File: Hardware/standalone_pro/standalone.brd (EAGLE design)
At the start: 110 x 100 mm, 107 parts, among them IC1 STM32F050C6T6A, IC2 AP1212, IC3 AP1212, Q2 32.768khz, U1 NMOS_2N7002, U10 ZXCT1107SA-7, U2 DMS3016SSS-13, U3 DMS3016SSS-13, U4 LM2576S, U5 NMOS_2N7002, U6 NMOS_2N7002, U7 INA213AIDCKT, U9 PMOS_RSS090P03, X1 KUSBVX, X2 KUSBVX, X3 KUSBVX, X4 KUSBVX

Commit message: Pro Standalone board updated
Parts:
- removed 5V_CIN: 100u, resistor:PANASONIC_E
- removed 5V_COUT: 1000uF, resistor:PANASONIC_G
- removed GATE_DRIVE: IR2104S, equinox:IR2104S
- removed KEY_1, KEY_2, KEY_3: 10K, rcl:M0805
- removed Q2: 32.768khz, equinox:CRYSTAL_CMJ206T
- removed U$2, U$3, U$4, U$5, U$6: KYCON_KLDVX-0202, equinox:KYCON_KLVDX_2020_B
- removed U1: NMOS_2N7002, equinox:SOT103P240X110-3N
- added C21: 100uF, resistor:PANASONIC_E
- added C22: 1000uF, resistor:PANASONIC_G
- added D1: SSB43L, equinox:DO214AA
- added D5: BZX384-C3V6, equinox:SOD323
- added DC1, DC2, DC3, DC4, DC5: KYCON_KLDVX-0202, equinox:KYCON_KLVDX_2020_B
- added IC4: AP1212, equinox:SO8
- added PTC1: 7A, equinox:PTC_MF_R700
- added Q1: 32.768khz, equinox:CRYSTAL_CMJ206T
- added R38: 49.9k, resistor:M0805
- added U11, U12, U8: NMOS_2N7002, equinox:SOT103P240X110-3N
- BUZZ1: device buzzer:14MM_5M_PINS -> equinox:BUZZ_14MM_5M_PINS
- C5: value 0.1uF -> 100nF
- D3: value (none) -> SSB43L
- D4: value US1D - 1625280 -> US1D
- IC3: value AP1212 -> IR2104S; device equinox:SO8 -> equinox:IR2104S
- R1: value 1k -> 75k
- R21: value 1K -> 1k
- R29: value 75k -> 1k
- R31: value 49.9k -> 10M
- R32, R34, R36: value 75k -> 49.9k
- R33, R35, R37: value 49.9k -> 75k
- R4, R6: value 1.32k -> 1.33k
- U2, U3: value DMS3016SSS-13 -> FDS6690a
- moved U4 123.5 mm to (-4.25, 12.2), flipped to the bottom
- moved L_5V 118.2 mm to (-3.00, 38.0), flipped to the bottom
- moved DIS1 106.2 mm to (-3.10, 56.0), flipped to the top
- moved C11 105.0 mm to (-8.00, 69.0), flipped to the bottom
- moved R1 99.8 mm to (-6.00, -18.0), turned to 0 degrees
- moved IC3 97.1 mm to (9.00, 65.0), flipped to the bottom
- moved C2 95.0 mm to (-3.00, 66.0), flipped to the bottom
- moved D2 95.0 mm to (-3.00, 69.0), flipped to the bottom
- moved D4 95.0 mm to (-3.00, 62.0), flipped to the bottom
- moved R29 90.0 mm to (15.0, 51.0), flipped to the bottom
- moved JTAG 86.0 mm to (92.0, 18.0), flipped to the bottom
- moved X3 86.0 mm to (7.00, 25.6), flipped to the top
- moved U2 83.0 mm to (3.00, 75.0), flipped to the bottom
- moved KEYPAD 82.0 mm to (91.0, 36.0), flipped to the bottom
- moved LED1 82.0 mm to (92.0, 7.00), flipped to the bottom
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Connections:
- removed net LCD_PWR: IC1.32, R1.2
- new net N$47: R35.1, R36.2, X4.2
- new net N$48: R37.1, R38.2, X4.3
- net +3V3: no longer KEY_1.2, KEY_2.2, KEY_3.2
- net +5V: now also C22.+, IC4.7; no longer 5V_COUT.+, IC3.7
- net 12V_OUT: now also DC1.1, DC2.1, DC3.1; no longer U$2.1, U$3.1, U$4.1
- net 12V_OUT1: now also DC4.1, DC5.1; no longer U$5.1, U$6.1
- net GND: now also C21.-, C22.-, CONTR.1, D1.A, D5.A, DC1.2, DC1.3, DC2.2, DC2.3, DC3.2, DC3.3, DC4.2, DC4.3, DC5.2, DC5.3, DIS1.1, DIS1.10, DIS1.7, DIS1.8, DIS1.9, IC3.4, IC4.6, Q1.CASE, R32.1, R34.1, R36.1, R38.1, U11.2, U8.2; no longer 5V_CIN.-, 5V_COUT.-, BUZZ1.P$2, GATE_DRIVE.4, IC3.6, Q2.CASE, R31.1, R33.1, R35.1, R37.1, U$4.2, U$5.2, U$5.3, U$6.2, U$6.3, U1.2
- net N$1: now also Q1.P$2; no longer Q2.P$2
- net N$10: now also IC3.8; no longer GATE_DRIVE.8
- net N$13: now also IC3.5; no longer GATE_DRIVE.5
- net N$16: now also IC3.1; no longer GATE_DRIVE.1
- net N$17: now also R33.1, R34.2, X3.3; no longer R1.1, U1.1
- net N$18: now also Q1.P$3; no longer Q2.P$3
- net N$22: now also R29.1; no longer BUZZ1.P$1
- net N$23: no longer KEY_1.1
- net N$24: no longer KEY_2.1
- net N$26: no longer KEY_3.1
- net N$3: now also IC3.3; no longer GATE_DRIVE.3
- net N$4: now also D1.C, PTC1.P$1; no longer BATT.P$1
- net N$42: now also BUZZ1.P$2, U8.3; no longer R29.1, R31.2, X3.2
- net N$43: now also R29.2, U8.1; no longer R32.1, R33.2, X3.3
- net N$44: now also C16.2, R31.2, U11.1; no longer R34.1, R35.2, X4.2
- net N$45: now also U11.3, U12.2; no longer R36.1, R37.2, X4.3
- net N$46: now also BATT.P$1, PTC1.P$2; no longer U$2.2, U$2.3, U$3.2, U$3.3, U$4.3
- net N$5: now also R1.1, R32.2, X3.2; no longer CONTR.1, DIS1.1, DIS1.10, DIS1.7, DIS1.8, DIS1.9, U1.3
- net N$6: now also IC3.6; no longer GATE_DRIVE.6
- net N$7: now also IC3.7; no longer GATE_DRIVE.7
- net N$8: now also IC3.2; no longer GATE_DRIVE.2
- net NRST: now also U12.3
- net SOL_I: now also D5.C
- net USB_EN1: now also IC4.1; no longer IC3.1
- net USB_EN2: now also IC4.4; no longer IC3.4
- net USB_FLG1: now also IC4.2; no longer IC3.2
- net USB_FLG2: now also IC4.3; no longer IC3.3
- net USB_OUT1: now also IC4.8, R1.2, R33.2; no longer IC3.8, R29.2, R32.2
- net USB_OUT2: now also IC4.5, R35.2, R37.2; no longer IC3.5, R34.2, R36.2
- net V_BACKUP: no longer C16.2
- net V_LOAD: now also BUZZ1.P$1, C21.+; no longer 5V_CIN.+
- net WKUP: now also R31.1, U12.1
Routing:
- net V_LOAD: track 316.3 -> 8.97 mm, vias 16 -> 0
- net +5V: track 219.2 -> 0.00 mm, vias 4 -> 0
- net N$21: track 112.7 -> 0.00 mm
- net LCD_PWR: track 51.6 -> 0.00 mm, vias 2 -> 0
- net N$5: track 38.6 -> 0.00 mm, vias 1 -> 0
- net V_BACKUP: track 26.3 -> 55.8 mm, vias 0 -> 1
- net N$12: track 36.5 -> 62.3 mm
- net N$4: track 7.80 -> 30.9 mm
- net NRST: track 53.1 -> 73.8 mm, vias 0 -> 2
- net BATT_V: track 36.8 -> 54.0 mm
- net N$26: track 38.7 -> 25.9 mm
- net N$16: track 148.2 -> 160.5 mm
- net SOL_I: track 74.7 -> 86.7 mm
- net GND: track 76.7 -> 65.2 mm, vias 49 -> 28
- net N$6: track 66.1 -> 54.6 mm
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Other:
- board size 110 x 100 mm -> 110.1 x 100 mm
- board text added: "Designed by Ashley Grealish in London Manufactured in China"
- board text added: "GND"
- board text added: "RX"
- board text added: "TX"
- board text removed: "Design by Ashley Grealish - 2013"

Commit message: Added Relay to Standalone Pro
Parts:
- removed R14: 100K, rcl:M0805
- removed U9: PMOS_RSS090P03, equinox:SO8
- added D7: US1D, diode:DO-214AC
- added U$2: RELAY_G5RL-1E, equinox:G5RL-1E
- added U$3: CON_MOLEX_39_29_1028, equinox:MOLEX_39_29_1028
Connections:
- removed net N$25: R14.1, U5.3, U9.4
- new net N$50: D7.A, U$2.COIL+, U5.3
- net 12V_OUT: now also U$2.NO@1, U$2.NO@2, U$3.P$1; no longer U9.5, U9.6, U9.7, U9.8
- net GND: now also U$3.P$2
- net V_LOAD: now also D7.C, U$2.COM@1, U$2.COM@2; no longer R14.2, U9.1, U9.2, U9.3
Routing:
- net N$25: track 13.3 -> 0.00 mm
- net 12V_OUT: track 71.2 -> 58.7 mm
- net V_LOAD: track 8.97 -> 5.40 mm

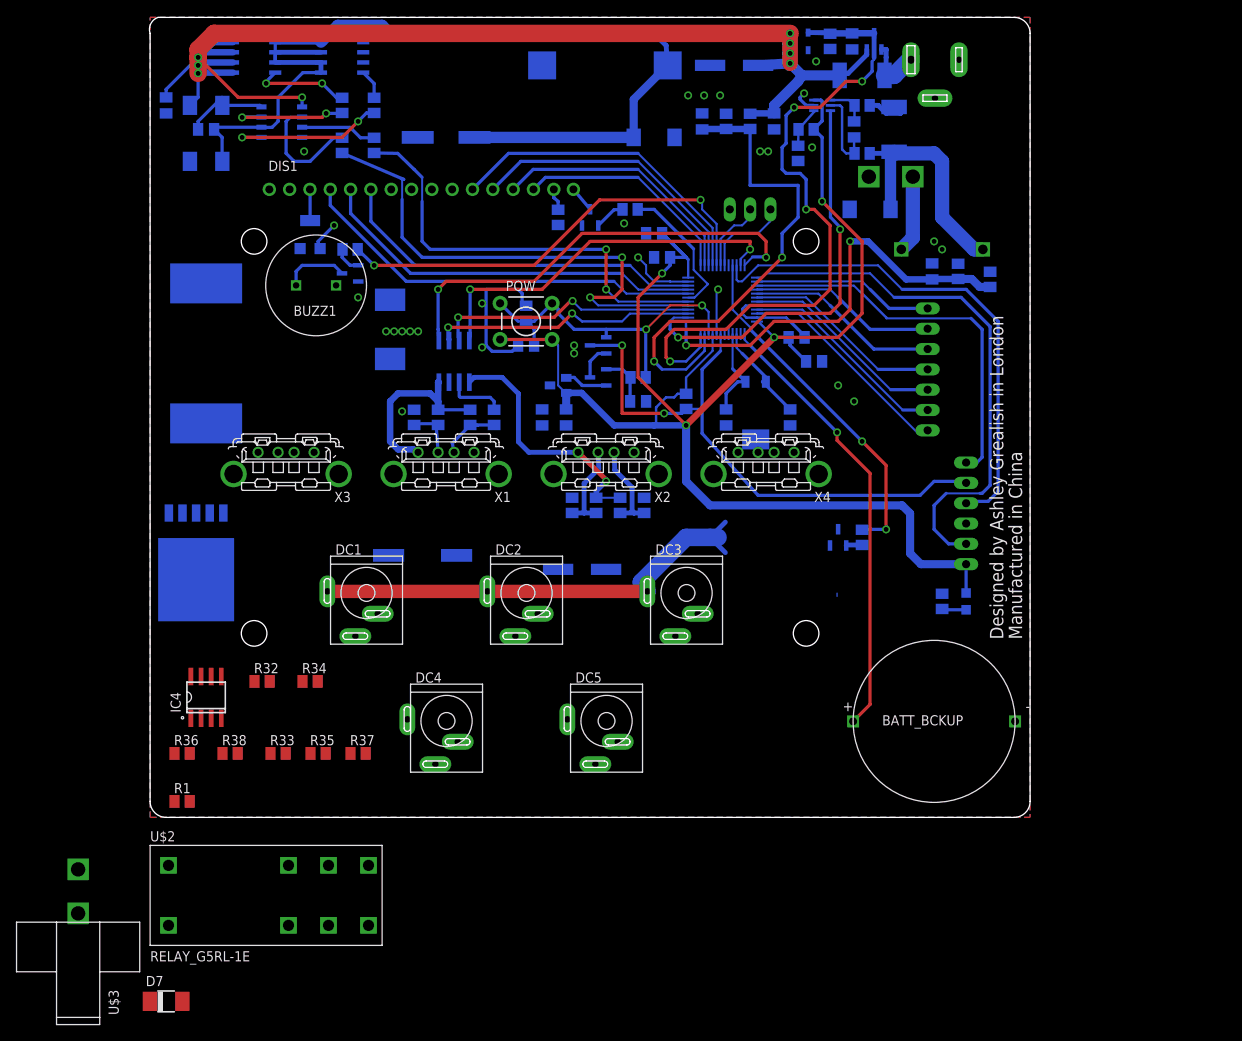
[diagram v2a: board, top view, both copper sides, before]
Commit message: Connections added (with corrected faults)
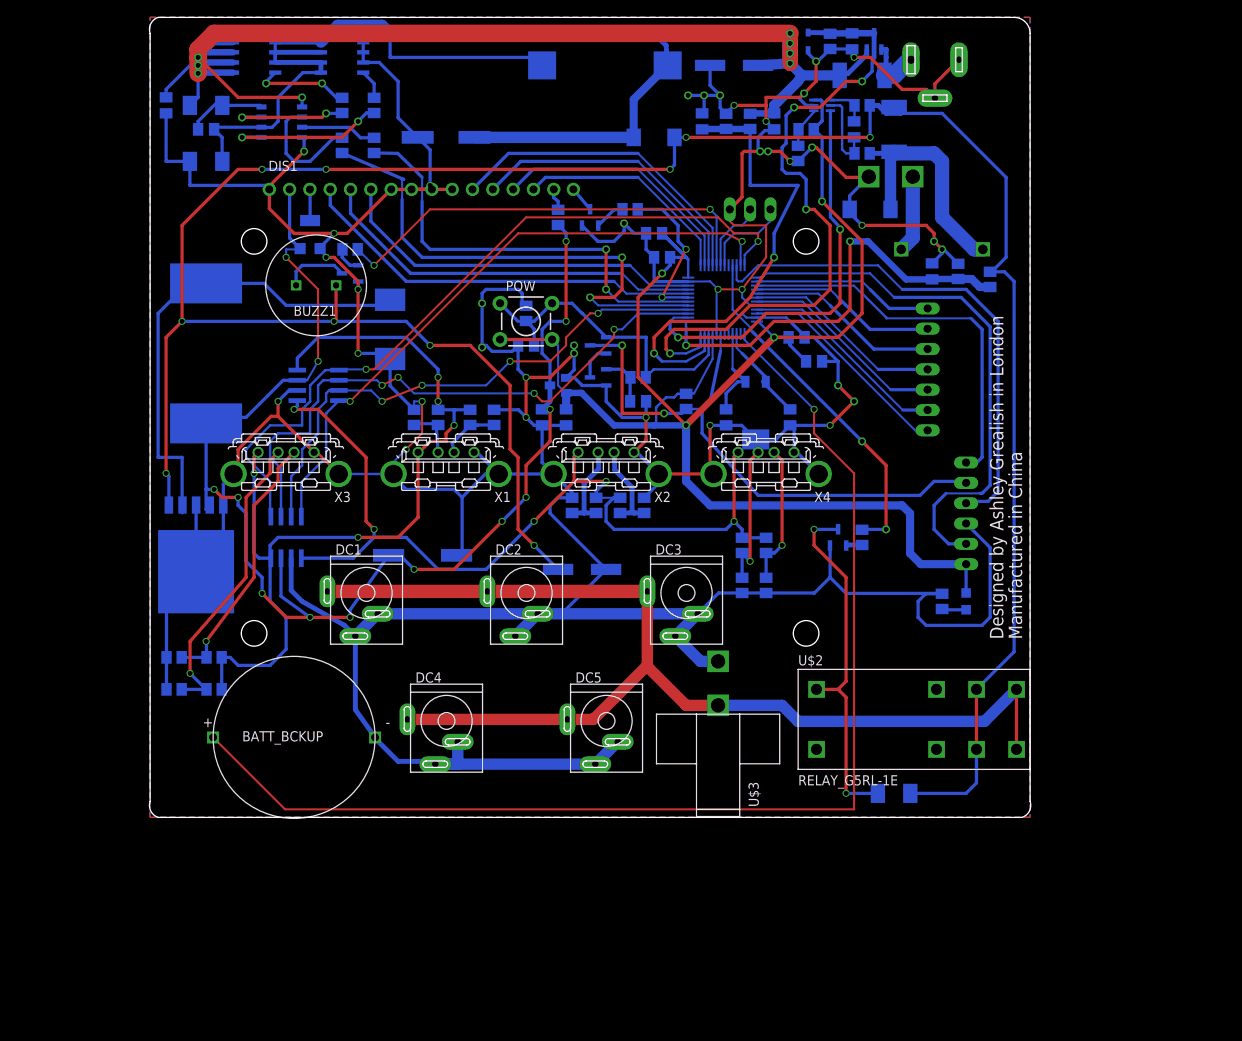
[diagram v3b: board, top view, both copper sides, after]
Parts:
- moved D7 94.6 mm to (83.0, -17.0), flipped to the bottom
- moved U$3 84.1 mm to (61.0, -6.00)
- moved U$2 83.9 mm to (84.0, -8.00)
- moved BATT_BCKUP 80.0 mm to (8.00, -10.0)
- moved R36 73.1 mm to (64.0, 9.00), flipped to the bottom, turned to 90 degrees
- moved R38 70.2 mm to (67.0, 9.00), flipped to the bottom, turned to 90 degrees
- moved R35 59.0 mm to (64.0, 14.0), flipped to the bottom, turned to 90 degrees
- moved R37 57.2 mm to (67.0, 14.0), flipped to the bottom, turned to 90 degrees
- moved IC4 22.4 mm to (7.00, 15.0), flipped to the bottom, turned to 180 degrees
- moved IC2 17.3 mm to (11.0, 34.0), turned to 270 degrees
- moved R34 17.3 mm to (-7.00, 0.00), flipped to the bottom, turned to 180 degrees
- moved R1 14.6 mm to (-2.00, -4.00), flipped to the bottom, turned to 180 degrees
- moved R33 14.4 mm to (-2.00, 0.00), flipped to the bottom, turned to 180 degrees
- moved R32 11.0 mm to (-7.00, -4.00), flipped to the bottom, turned to 180 degrees
- moved U4 1.00 mm to (-4.25, 13.2)
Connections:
- removed net 12V_OUT1: DC4.1, DC5.1
- net 12V_OUT: now also DC4.1, DC5.1
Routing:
- net GND: track 65.2 -> 776.5 mm, vias 28 -> 38
- net V_LOAD: track 5.40 -> 318.5 mm, vias 0 -> 10
- net +5V: track 0.00 -> 164.5 mm, vias 0 -> 13
- net V_BACKUP: track 55.8 -> 148.9 mm
- net USB_OUT1: track 24.4 -> 109.8 mm, vias 0 -> 5
- net 12V_OUT: track 58.7 -> 140.3 mm
- net USB_OUT2: track 31.9 -> 113.2 mm, vias 1 -> 5
- net N$21: track 0.00 -> 60.8 mm
- net N$50: track 0.00 -> 45.2 mm, vias 0 -> 2
- net USB_FLG1: track 33.5 -> 75.2 mm, vias 2 -> 4
- net N$5: track 0.00 -> 37.9 mm, vias 0 -> 1
- net USB_EN1: track 55.9 -> 93.5 mm
- net USB_FLG2: track 33.0 -> 68.1 mm, vias 2 -> 4
- net N$17: track 0.00 -> 32.8 mm, vias 0 -> 1
- net USB_EN2: track 47.4 -> 78.9 mm
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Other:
- board size 110.1 x 100 mm -> 110.2 x 100 mm

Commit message: Components on correct side and gnd ripped up
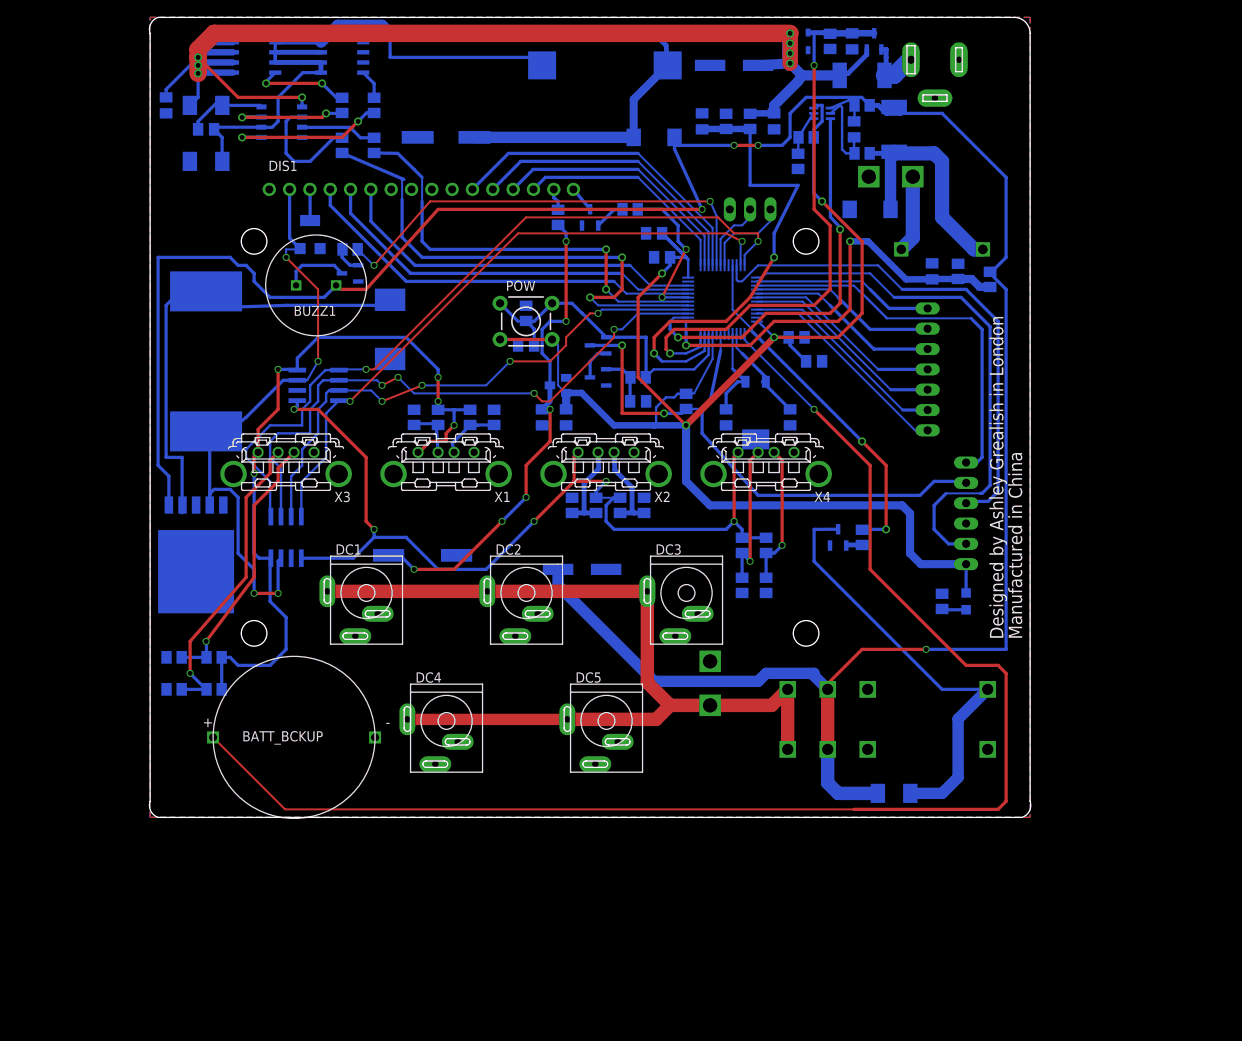
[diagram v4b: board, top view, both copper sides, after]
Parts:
- moved L_5V 1.00 mm to (-3.00, 37.0)
- moved R25 1.00 mm to (72.0, 65.0)
- moved R26 1.00 mm to (71.0, 62.0)
- moved U$3 1.00 mm to (60.0, -6.00), flipped to the bottom
- moved U7 1.00 mm to (74.0, 68.0)
- turned D7 to 180 degrees
- flipped U$2 to the bottom
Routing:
- net GND: track 776.5 -> 0.00 mm, vias 38 -> 0
- net V_BACKUP: track 148.9 -> 177.6 mm
- net 12V_OUT: track 140.3 -> 112.0 mm
- net +5V: track 164.5 -> 140.1 mm, vias 13 -> 10
- net USB_OUT1: track 109.8 -> 93.9 mm
- net SOL_I: track 85.1 -> 74.0 mm, vias 4 -> 2
- net N$50: track 45.2 -> 54.5 mm, vias 2 -> 0
- net V_LOAD: track 318.5 -> 314.3 mm, vias 10 -> 4
- net N$39: track 5.19 -> 6.78 mm
- net N$21: track 60.8 -> 59.3 mm
- net N$22: track 55.1 -> 56.7 mm
- net BATT_I: track 51.4 -> 50.4 mm

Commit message: Drc; overlap errors corrected
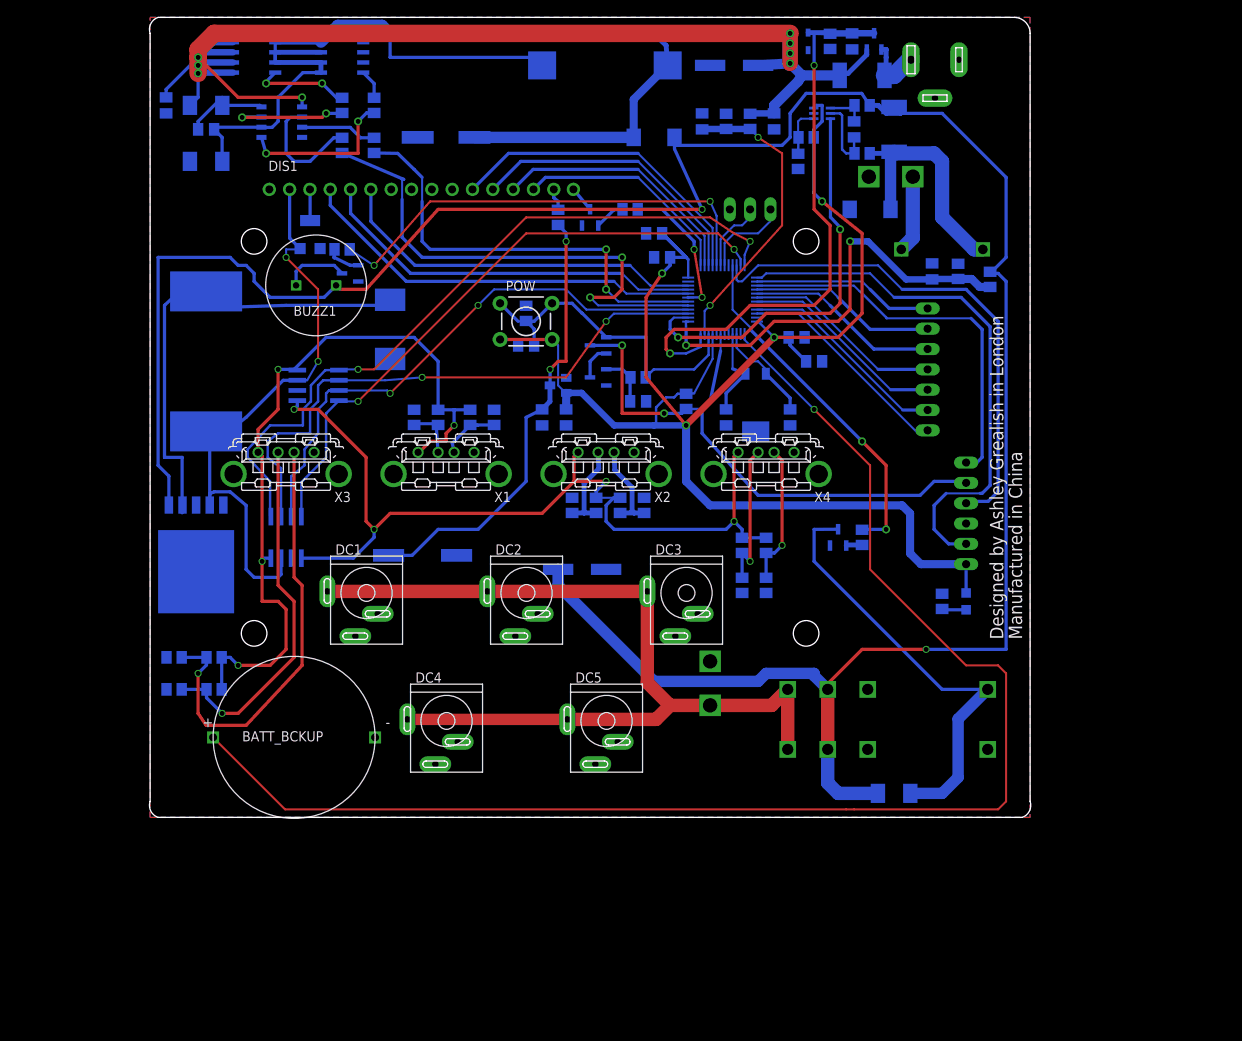
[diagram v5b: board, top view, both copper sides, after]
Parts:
- moved Q1 1.00 mm to (66.0, 32.0)
- moved R29 1.00 mm to (14.0, 51.0)
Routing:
- net SOL_V: track 59.9 -> 37.4 mm
- net N$17: track 32.8 -> 54.6 mm
- net +5V: track 140.1 -> 130.7 mm, vias 10 -> 4
- net N$5: track 37.9 -> 45.3 mm
- net USB_OUT2: track 113.2 -> 109.5 mm, vias 5 -> 4
- net USB_EN1: track 93.5 -> 90.7 mm
- net USB_FLG1: track 75.2 -> 72.8 mm, vias 4 -> 2
- net V_LOAD: track 314.3 -> 316.7 mm, vias 4 -> 2
- net LCD_BK_EN: track 19.3 -> 17.6 mm
- net USB_OUT1: track 93.9 -> 95.4 mm, vias 5 -> 4
- net N$41: track 11.0 -> 9.59 mm
- net USB_EN2: track 78.9 -> 77.6 mm
- net USB_FLG2: track 68.1 -> 69.2 mm, vias 4 -> 2
- net +3V3: track 209.8 -> 208.9 mm
- net N$43: track 3.44 -> 4.35 mm
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
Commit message: Gnd connected
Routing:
- net GND: track 0.00 -> 30.9 mm, vias 0 -> 14
- net +5V: track 130.7 -> 153.9 mm
